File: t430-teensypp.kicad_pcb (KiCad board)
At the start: 2 copper layers, 21 parts, among them U1 Teensy++, U2 MCP1700-3302E_SOT23, X1 T430

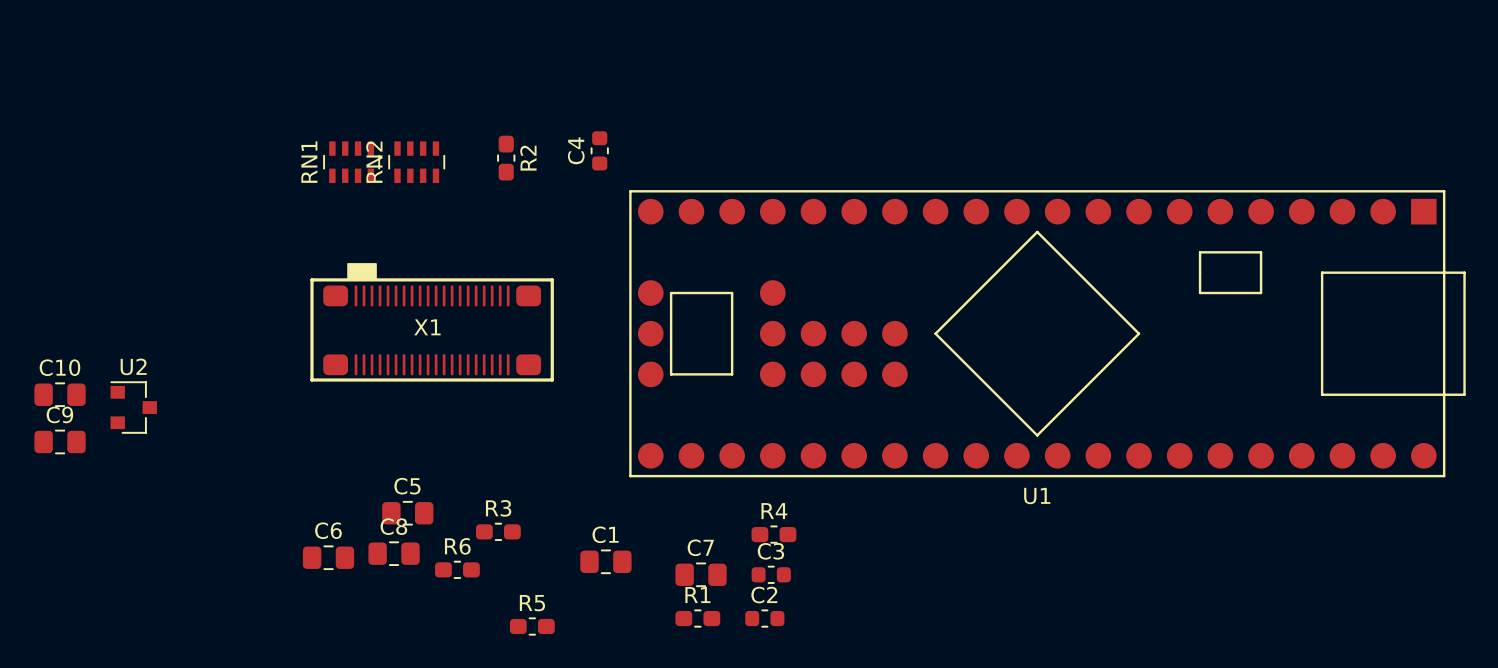
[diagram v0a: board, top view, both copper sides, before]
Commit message: Started mapping traces
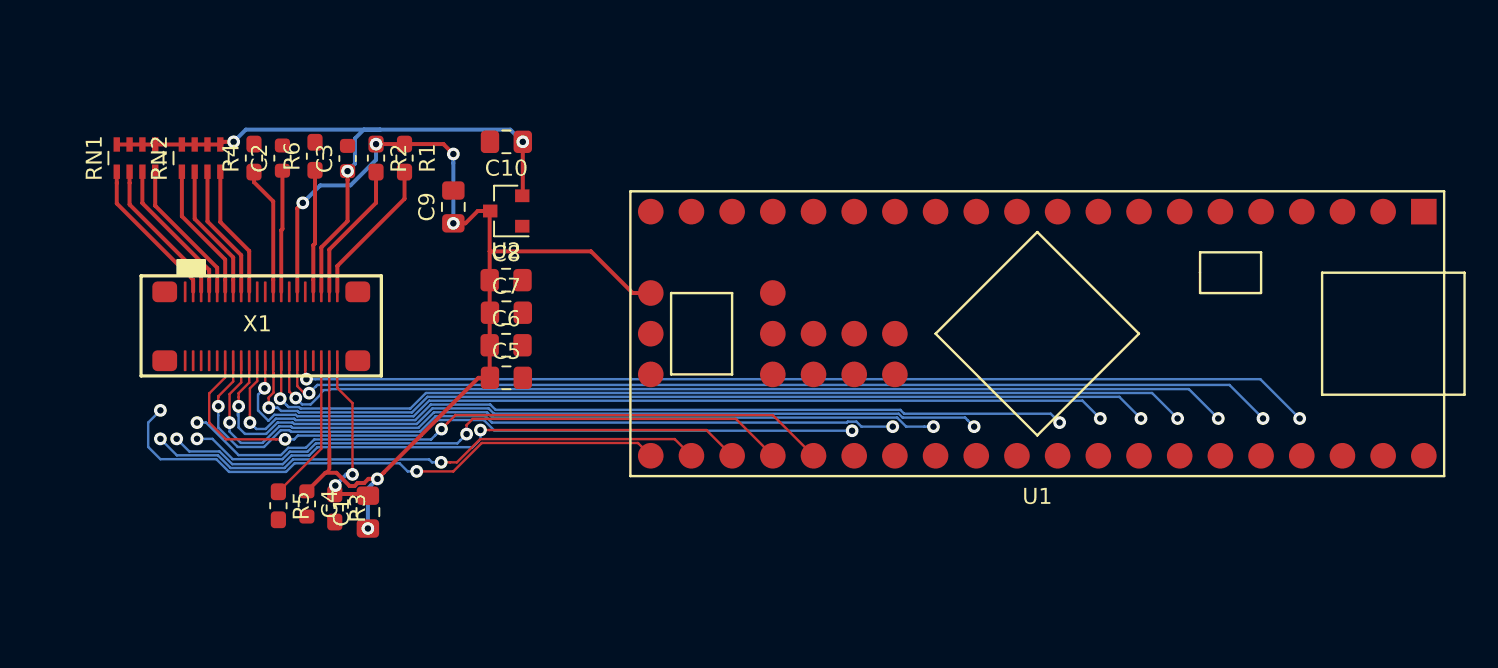
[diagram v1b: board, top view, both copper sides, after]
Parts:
- moved C2 41.6 mm to (172.5, 69.1), turned to 90 degrees
- moved R4 40.1 mm to (170.7, 69.1), turned to 90 degrees
- moved C3 37.1 mm to (176.5, 69.1), turned to 90 degrees
- moved R1 34.1 mm to (180.1, 69.1), turned to 270 degrees
- moved C10 32.0 mm to (186.4, 68.1), turned to 180 degrees
- moved C4 28.6 mm to (174.0, 90.7), turned to 270 degrees
- moved C9 28.6 mm to (183.1, 72.1), turned to 90 degrees
- moved R6 27.3 mm to (174.5, 69.0), turned to 90 degrees
- moved U2 26.3 mm to (186.4, 72.4), turned to 180 degrees
- moved C7 20.4 mm to (186.4, 78.7)
- moved C8 18.5 mm to (186.4, 76.7)
- moved R5 17.6 mm to (172.2, 90.8), turned to 270 degrees
- moved C6 17.3 mm to (186.4, 80.8)
- moved C1 15.2 mm to (177.8, 91.2), turned to 90 degrees
- moved RN2 13.5 mm to (167.4, 69.1)
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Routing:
- net +5V: track 0.00 -> 75.3 mm, vias 0 -> 6
- net /t430-connector/COL13: track 0.00 -> 64.2 mm, vias 0 -> 2
- net /t430-connector/COL15: track 0.00 -> 63.1 mm, vias 0 -> 2
- net /t430-connector/COL12: track 0.00 -> 61.4 mm, vias 0 -> 2
- net /t430-connector/COL14: track 0.00 -> 59.7 mm, vias 0 -> 2
- net /t430-connector/COL11: track 0.00 -> 58.6 mm, vias 0 -> 2
- net /t430-connector/COL0: track 0.00 -> 57.2 mm, vias 0 -> 2
- net /t430-connector/COL9: track 0.00 -> 55.9 mm, vias 0 -> 2
- net /t430-connector/COL1: track 0.00 -> 52.3 mm, vias 0 -> 2
- net /t430-connector/COL10: track 0.00 -> 50.2 mm, vias 0 -> 2
- net /t430-connector/COL2: track 0.00 -> 48.4 mm, vias 0 -> 2
- net /t430-connector/COL7: track 0.00 -> 45.6 mm, vias 0 -> 2
- net +3V3: track 0.00 -> 41.7 mm, vias 0 -> 3
- net /Teensy2.0++/COL15: track 0.00 -> 41.4 mm, vias 0 -> 2
- net /Teensy2.0++/~KBD_BL_DETECT: track 0.00 -> 38.8 mm, vias 0 -> 2
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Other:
- net class Default: clearance 0.2 -> 0.0889; trace_width 0.25 -> 0.1524
- rule trace_clearance: 0.2 -> 0.0889
- rule trace_min: 0.2 -> 0.0889
- rule via_min_drill: 0.3 -> 0.2032
- rule via_min_size: 0.4 -> 0.4572

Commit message: Routed to 6/6
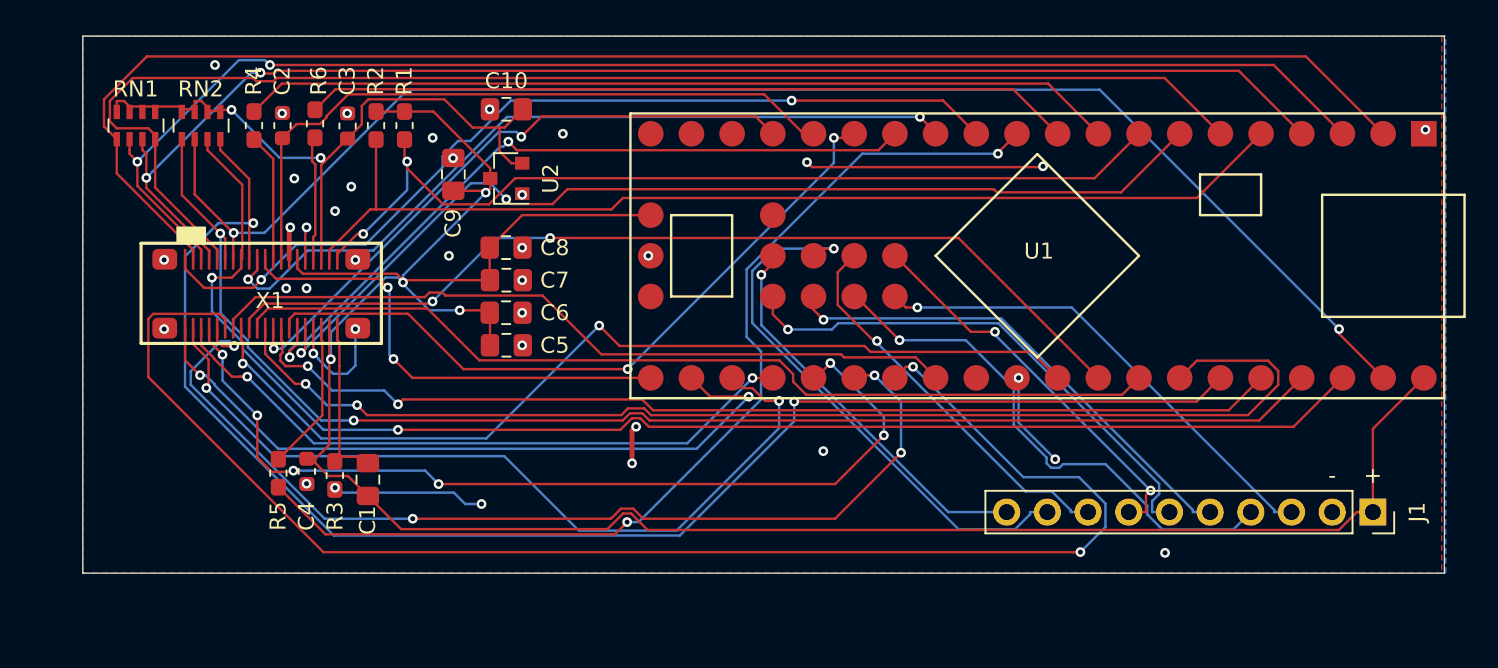
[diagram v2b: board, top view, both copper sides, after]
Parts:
- added J1: Conn_01x10, Connector_PinSocket_2.54mm:PinSocket_1x10_P2.54mm_Vertical, F.Cu at (240.5, 91.2)
- moved U1 4.86 mm to (219.6, 75.2)
- moved X1 2.03 mm to (171.1, 77.7)
- moved R3 2.03 mm to (175.7, 88.9)
- moved C1 2.03 mm to (177.8, 89.2)
- moved C6 2.03 mm to (186.4, 78.7)
- moved C10 2.03 mm to (186.4, 66.0)
- moved C2 2.03 mm to (172.5, 67.1)
- moved C3 2.03 mm to (176.5, 67.1)
- moved C4 2.03 mm to (174.0, 88.6)
- moved C5 2.03 mm to (186.4, 80.8)
- moved C7 2.03 mm to (186.4, 76.7)
- moved C8 2.03 mm to (186.4, 74.7)
- moved C9 2.03 mm to (183.1, 70.1)
- moved R1 2.03 mm to (180.1, 67.1)
- moved R2 2.03 mm to (178.3, 67.1)
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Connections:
- C2 pad 1: /t430-connector/KBD_BL_PWM -> /Teensy2.0++/KBD_BL_PWM
- R1 pad 2: /t430-connector/TP_CLK -> /Teensy2.0++/TP_CLK
- R2 pad 2: /t430-connector/TP_DATA -> /Teensy2.0++/TP_DATA
- R4 pad 2: /t430-connector/LED_PWR -> /Teensy2.0++/LED_PWR
- R5 pad 2: /t430-connector/LED_MICMUTE -> /Teensy2.0++/LED_MICMUTE
- R6 pad 2: /t430-connector/LED_MUTE -> /Teensy2.0++/LED_MUTE
- RN1 pad 1: /t430-connector/ROW5 -> /Teensy2.0++/ROW5
- RN1 pad 2: /t430-connector/ROW0 -> /Teensy2.0++/ROW0
- RN1 pad 3: /t430-connector/ROW3 -> /Teensy2.0++/ROW3
- RN1 pad 4: /t430-connector/ROW2 -> /Teensy2.0++/ROW2
- RN2 pad 1: /t430-connector/ROW4 -> /Teensy2.0++/ROW4
- RN2 pad 2: /t430-connector/ROW1 -> /Teensy2.0++/ROW1
- RN2 pad 3: /t430-connector/ROW6 -> /Teensy2.0++/ROW6
- RN2 pad 4: /t430-connector/ROW7 -> /Teensy2.0++/ROW7
- U1 pad 10: /Teensy2.0++/COL2 -> /Teensy2.0++/LED_MUTE
- U1 pad 12: /Teensy2.0++/LED_MUTE -> /Teensy2.0++/~HOTKEY
- U1 pad 13: /Teensy2.0++/COL3 -> /Teensy2.0++/~PWR_SWITCH
- U1 pad 14: /Teensy2.0++/COL4 -> /Teensy2.0++/COL15
- U1 pad 15: /Teensy2.0++/COL5 -> /Teensy2.0++/COL12
- U1 pad 17: /Teensy2.0++/COL6 -> /Teensy2.0++/COL11
- U1 pad 18: /Teensy2.0++/COL7 -> Net-(U1-Pad18)
- U1 pad 19: /Teensy2.0++/COL8 -> Net-(U1-Pad19)
- U1 pad 2: /Teensy2.0++/ROW7 -> /Teensy2.0++/ROW5
- U1 pad 20: /Teensy2.0++/COL9 -> Net-(U1-Pad20)
- U1 pad 24: Net-(U1-Pad24) -> /Teensy2.0++/~KBD_BL_DETECT
- U1 pad 25: Net-(U1-Pad25) -> /Teensy2.0++/COL4
- U1 pad 26: Net-(U1-Pad26) -> /Teensy2.0++/COL5
- U1 pad 27: /Teensy2.0++/~KBD_BL_DETECT -> /Teensy2.0++/COL8
- U1 pad 28: /Teensy2.0++/COL15 -> /Teensy2.0++/COL6
- U1 pad 29: /Teensy2.0++/COL14 -> /Teensy2.0++/COL3
- U1 pad 3: /Teensy2.0++/~HOTKEY -> /Teensy2.0++/ROW0
- U1 pad 30: /Teensy2.0++/COL13 -> /Teensy2.0++/COL7
- U1 pad 31: /Teensy2.0++/COL12 -> /Teensy2.0++/COL2
- U1 pad 34: /Teensy2.0++/COL11 -> /Teensy2.0++/COL10
- U1 pad 35: /Teensy2.0++/COL10 -> /Teensy2.0++/COL1
- U1 pad 36: /Teensy2.0++/ROW0 -> /Teensy2.0++/COL9
- U1 pad 37: /Teensy2.0++/ROW1 -> /Teensy2.0++/COL0
- U1 pad 38: /Teensy2.0++/ROW2 -> /Teensy2.0++/ROW7
- U1 pad 39: /Teensy2.0++/ROW3 -> /Teensy2.0++/COL14
- U1 pad 4: /Teensy2.0++/~PWR_SWITCH -> /Teensy2.0++/ROW3
- U1 pad 41: /Teensy2.0++/ROW5 -> /Teensy2.0++/ROW6
- U1 pad 42: /Teensy2.0++/ROW6 -> /Teensy2.0++/ROW1
- U1 pad 44: Net-(U1-Pad44) -> /Teensy2.0++/PA0
- U1 pad 45: Net-(U1-Pad45) -> /Teensy2.0++/PA1
- U1 pad 46: Net-(U1-Pad46) -> /Teensy2.0++/PA2
- U1 pad 47: Net-(U1-Pad47) -> /Teensy2.0++/PA3
- U1 pad 48: Net-(U1-Pad48) -> /Teensy2.0++/PA4
- U1 pad 49: Net-(U1-Pad49) -> /Teensy2.0++/PA5
- U1 pad 50: Net-(U1-Pad50) -> /Teensy2.0++/PA6
- U1 pad 51: Net-(U1-Pad51) -> /Teensy2.0++/PA7
- U1 pad 6: /Teensy2.0++/COL0 -> /Teensy2.0++/ROW2
- U1 pad 7: /Teensy2.0++/COL1 -> /Teensy2.0++/COL13
- X1 pad 1: /t430-connector/~HOTKEY -> /Teensy2.0++/~HOTKEY
- X1 pad 10: /t430-connector/COL3 -> /Teensy2.0++/COL3
- X1 pad 11: /t430-connector/ROW4 -> /Teensy2.0++/ROW4
- X1 pad 12: /t430-connector/COL7 -> /Teensy2.0++/COL7
- X1 pad 13: /t430-connector/ROW1 -> /Teensy2.0++/ROW1
- X1 pad 14: /t430-connector/COL2 -> /Teensy2.0++/COL2
- X1 pad 15: /t430-connector/ROW6 -> /Teensy2.0++/ROW6
- X1 pad 16: /t430-connector/COL10 -> /Teensy2.0++/COL10
- X1 pad 17: /t430-connector/ROW7 -> /Teensy2.0++/ROW7
- X1 pad 18: /t430-connector/COL1 -> /Teensy2.0++/COL1
- X1 pad 19: /t430-connector/~PWR_SWITCH -> /Teensy2.0++/~PWR_SWITCH
- X1 pad 2: /t430-connector/COL4 -> /Teensy2.0++/COL4
- X1 pad 20: /t430-connector/COL9 -> /Teensy2.0++/COL9
- X1 pad 21: /t430-connector/~KBD_BL_DETECT -> /Teensy2.0++/~KBD_BL_DETECT
- X1 pad 22: /t430-connector/COL0 -> /Teensy2.0++/COL0
- X1 pad 24: /t430-connector/COL11 -> /Teensy2.0++/COL11
- X1 pad 25: /t430-connector/KBD_BL_PWM -> /Teensy2.0++/KBD_BL_PWM
- X1 pad 26: /t430-connector/COL14 -> /Teensy2.0++/COL14
- X1 pad 27: (no net) -> GND
- X1 pad 28: /t430-connector/COL12 -> /Teensy2.0++/COL12
- X1 pad 3: /t430-connector/ROW5 -> /Teensy2.0++/ROW5
- X1 pad 30: /t430-connector/COL15 -> /Teensy2.0++/COL15
- X1 pad 31: (no net) -> GND
- X1 pad 32: /t430-connector/COL13 -> /Teensy2.0++/COL13
- X1 pad 34: (no net) -> GND
- X1 pad 37: /t430-connector/TP_DATA -> /Teensy2.0++/TP_DATA
- X1 pad 39: /t430-connector/TP_CLK -> /Teensy2.0++/TP_CLK
- X1 pad 4: /t430-connector/COL5 -> /Teensy2.0++/COL5
- X1 pad 41: (no net) -> GND
- X1 pad 42: (no net) -> GND
- X1 pad 43: (no net) -> GND
- X1 pad 44: (no net) -> GND
- X1 pad 5: /t430-connector/ROW0 -> /Teensy2.0++/ROW0
- X1 pad 6: /t430-connector/COL8 -> /Teensy2.0++/COL8
- X1 pad 7: /t430-connector/ROW3 -> /Teensy2.0++/ROW3
- X1 pad 8: /t430-connector/COL6 -> /Teensy2.0++/COL6
- X1 pad 9: /t430-connector/ROW2 -> /Teensy2.0++/ROW2
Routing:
- net /Teensy2.0++/ROW5: track 0.00 -> 95.3 mm
- net /Teensy2.0++/ROW7: track 0.00 -> 95.0 mm, vias 0 -> 2
- net /Teensy2.0++/COL7: track 0.00 -> 92.6 mm, vias 0 -> 2
- net /Teensy2.0++/ROW1: track 0.00 -> 91.6 mm, vias 0 -> 2
- net /Teensy2.0++/ROW0: track 0.00 -> 89.1 mm, vias 0 -> 2
- net /Teensy2.0++/ROW6: track 0.00 -> 88.8 mm, vias 0 -> 2
- net /Teensy2.0++/ROW3: track 0.00 -> 85.8 mm, vias 0 -> 2
- net /Teensy2.0++/ROW4: track 0.00 -> 85.6 mm, vias 0 -> 2
- net /Teensy2.0++/ROW2: track 0.00 -> 85.3 mm
- net /Teensy2.0++/COL0: track 0.00 -> 75.3 mm, vias 0 -> 2
- net +5V: track 75.3 -> 150.2 mm, vias 6 -> 4
- net /Teensy2.0++/TP_DATA: track 0.00 -> 66.1 mm
- net /Teensy2.0++/COL14: track 0.00 -> 65.7 mm, vias 0 -> 2
- net /t430-connector/COL13: track 64.2 -> 0.00 mm, vias 2 -> 0
- net /Teensy2.0++/LED_MICMUTE: track 0.00 -> 63.8 mm, vias 0 -> 2
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- added copper zone on B.Cu, net GND
- added copper zone on F.Cu, net GND
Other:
- board outline added: 85 x 33.5 mm
- net class Default: clearance 0.0889 -> 0.1524; via_dia 0.8 -> 0.6096; via_drill 0.4 -> 0.3048
- rule trace_clearance: 0.0889 -> 0.1524
- rule trace_min: 0.0889 -> 0.1524
- rule via_min_drill: 0.2032 -> 0.3048
- rule via_min_size: 0.4572 -> 0.6096
- board text added: "+"
- board text added: "-"

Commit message: Add holes for Teensy
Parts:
- U1: footprint teensy:Teensy2.0++Pads -> teensy:Teensy2.0++
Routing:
- net GND: track 44.2 -> 36.5 mm, vias 38 -> 35
- net /Teensy2.0++/ROW1: track 91.6 -> 98.8 mm
- net /Teensy2.0++/PA0: track 30.4 -> 33.5 mm
- net /Teensy2.0++/COL5: track 51.5 -> 48.5 mm
- net /Teensy2.0++/COL8: track 41.0 -> 43.9 mm
- net /Teensy2.0++/LED_MICMUTE: track 63.8 -> 66.5 mm
- net /Teensy2.0++/COL7: track 92.6 -> 94.8 mm
- net /Teensy2.0++/PA6: track 34.7 -> 36.7 mm
- net /Teensy2.0++/PA2: track 31.0 -> 32.8 mm
- net /Teensy2.0++/PA7: track 24.8 -> 26.4 mm
- net /Teensy2.0++/PA3: track 33.0 -> 34.3 mm
- net /Teensy2.0++/COL2: track 47.3 -> 48.4 mm
- net /Teensy2.0++/PA1: track 33.3 -> 34.3 mm
- net /Teensy2.0++/COL12: track 44.4 -> 45.3 mm
- net /Teensy2.0++/ROW7: track 95.0 -> 94.3 mm
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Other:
- rule trace_min: 0.1524 -> 0.15
